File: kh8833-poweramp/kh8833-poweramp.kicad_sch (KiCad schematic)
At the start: 21 parts, among them J10 Conn_01x03, J11 Conn_01x03, J12 Conn_01x03, J7 Conn_01x03, J8 Conn_01x03, J9 Conn_01x06

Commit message: Add speaker protection
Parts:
- D1: value (none) -> KBU6B; footprint (none) -> Diode_THT:Diode_Bridge_Vishay_KBU
- F1: value (none) -> 2.5A; footprint (none) -> Fuse:Fuseholder_Littelfuse_100_series_5x20mm
- J1, J3, J5, J6: value (none) -> Conn_01x03; footprint (none) -> TerminalBlock_Phoenix:TerminalBlock_Phoenix_MKDS-1,5-3-5.08_1x03_P5.08mm_Horizontal
- J2, J4: value (none) -> Conn_01x02; footprint (none) -> TerminalBlock_Phoenix:TerminalBlock_Phoenix_MKDS-1,5-2-5.08_1x02_P5.08mm_Horizontal
- T1: value (none) -> Transformer_1P_SS_2P; footprint (none) -> TerminalBlock_Phoenix:TerminalBlock_Phoenix_MKDS-1,5-10-5.08_1x10_P5.08mm_Horizontal
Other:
- added sheet Protector de Parlantes (speakerprot.kicad_sch)
- moved on the sheet: C1, C2, C3, C4, D1, F1, F2, F3, J1, J10, J11, J12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

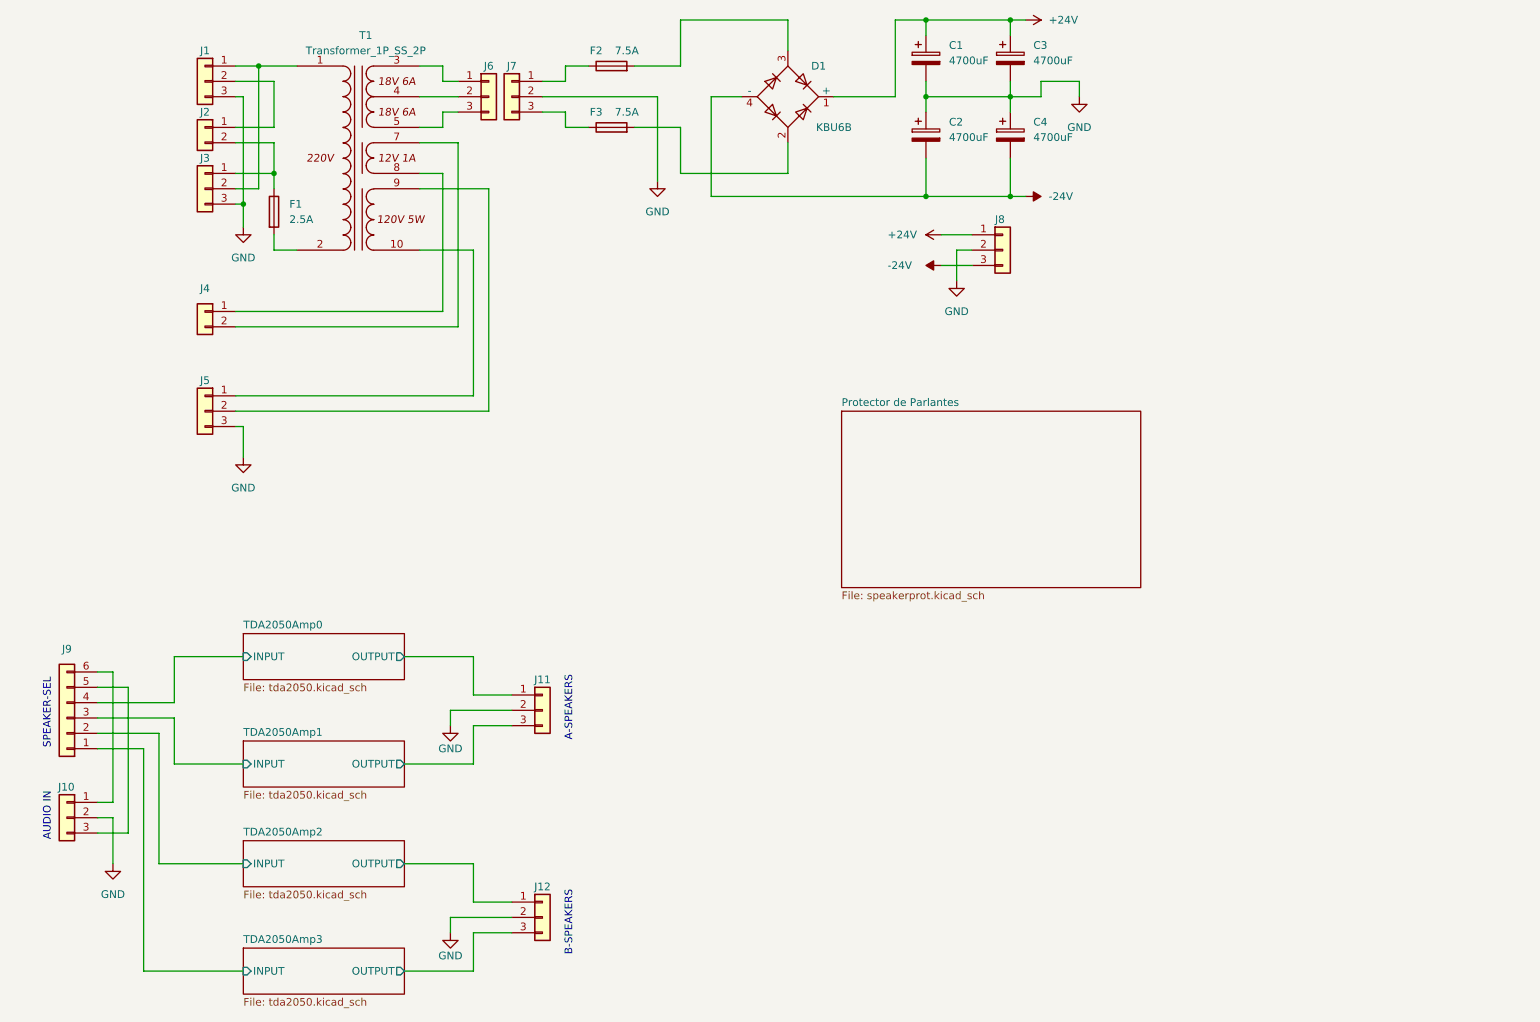
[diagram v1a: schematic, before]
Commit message: Add speaker prot - v1.0
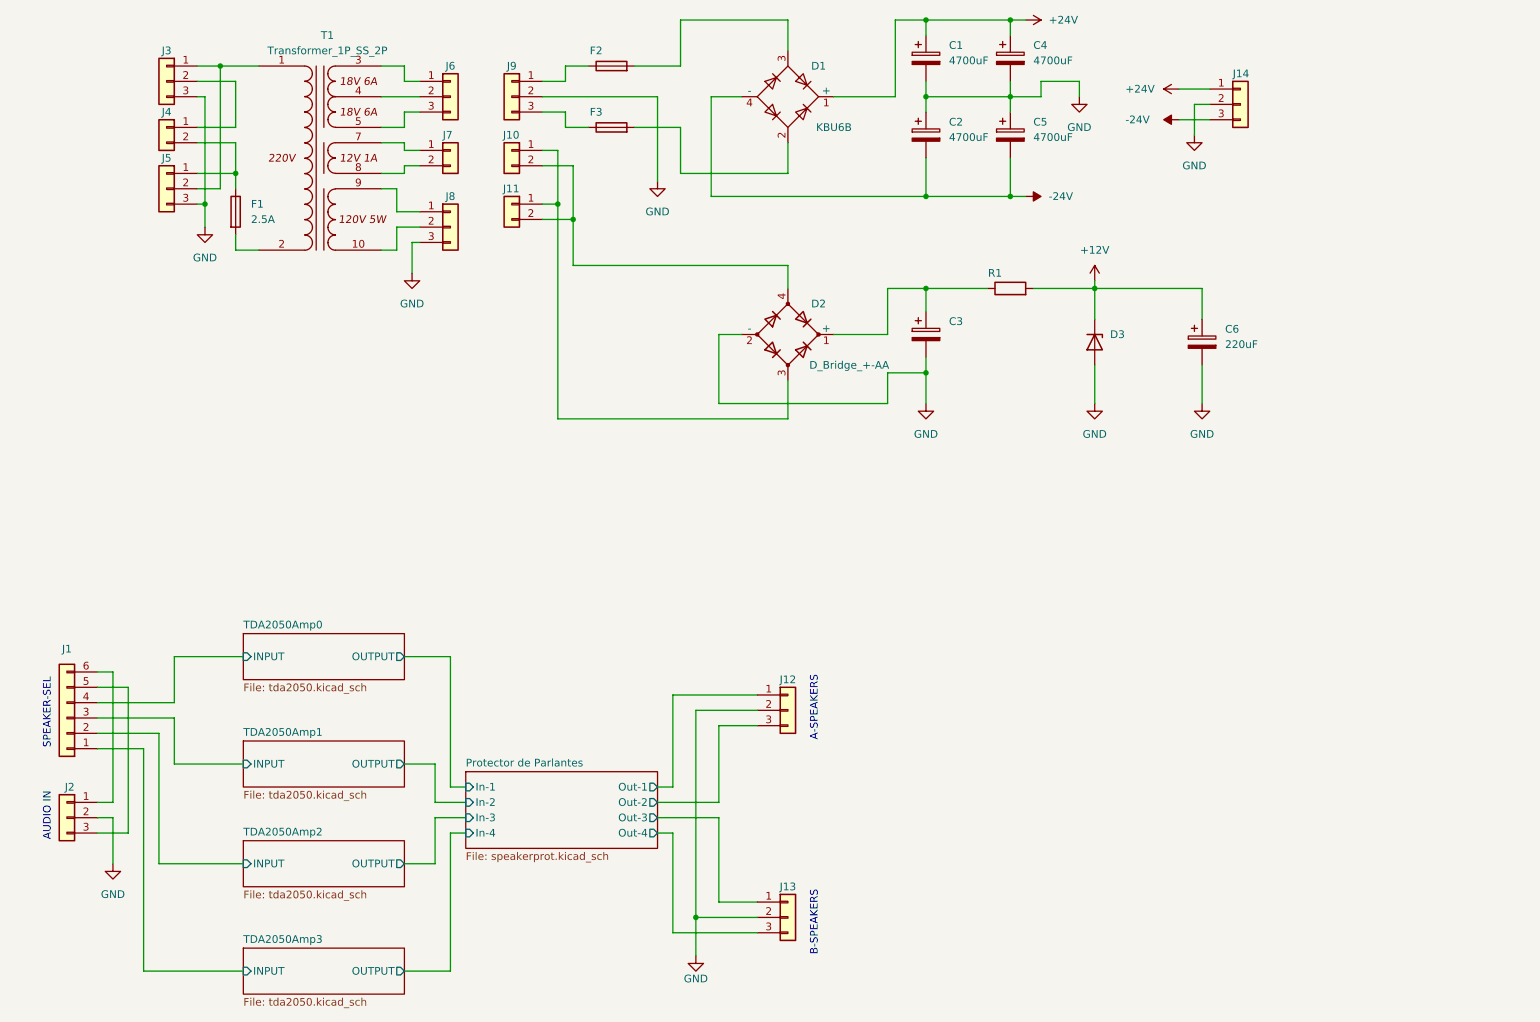
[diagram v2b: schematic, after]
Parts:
- added C3: (no value), Capacitor_THT:CP_Radial_D8.0mm_P5.00mm, symbol Device:C_Polarized
- added C6: 220uF, Capacitor_THT:CP_Radial_D8.0mm_P5.00mm, symbol Device:C_Polarized
- added D2: D_Bridge_+-AA, Diode_THT:Diode_Bridge_Round_D9.0mm, symbol Device:D_Bridge_+-AA
- added D3: (no value), symbol Diode:1N47xxA
- added J10, J11: (no value), symbol Connector_Generic:Conn_01x02
- added R1: (no value), Resistor_THT:R_Axial_DIN0207_L6.3mm_D2.5mm_P10.16mm_Horizontal, symbol Device:R
- F2, F3: value 7.5A -> (none); footprint Fuse:Fuseholder_Littelfuse_100_series_5x20mm -> (none)
- renumbered C3 to C4, C4 to C5, J9 to J1, J11 to J12, J12 to J13, J8 to J14, J10 to J2, J1 to J3, J2 to J4, J3 to J5, J4 to J7, J5 to J8, J7 to J9
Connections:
- net GND: now also C3.2, C6.2, D2.2 (-), D3.2 (A)
- net at T1.10 (SA): now also J8.2 (Pin_2); no longer J8.1 (Pin_1)
- net at T1.7 (SB): now also J7.1 (Pin_1); no longer J7.2 (Pin_2)
- net at T1.8 (SA): now also J7.2 (Pin_2); no longer J7.1 (Pin_1)
- net at T1.9 (SB): now also J8.1 (Pin_1); no longer J8.2 (Pin_2)
- net TDA2050Amp0/OUTPUT renamed Protector de Parlantes/Out-1
- net TDA2050Amp1/OUTPUT renamed Protector de Parlantes/Out-2
- net TDA2050Amp2/OUTPUT renamed Protector de Parlantes/Out-3
- net TDA2050Amp3/OUTPUT renamed Protector de Parlantes/Out-4
- new net: D2.3, J10.1 (Pin_1), J11.1 (Pin_1)
- new net: D2.4, J10.2 (Pin_2), J11.2 (Pin_2)
- new net: C3.1, D2.1 (+), R1.1
- new net +12V: C6.1, D3.1 (K), R1.2
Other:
- sheet Protector de Parlantes ports: added In-1, In-2, In-3, In-4, Out-1, Out-2, Out-3, Out-4; removed none
- moved on the sheet: F1, J12, J13, J14, J3, J4, J5, J6, J7, J8, T1
